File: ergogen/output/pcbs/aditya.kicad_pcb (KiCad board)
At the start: 2 copper layers, 133.2 x 110.8 mm, 58 parts

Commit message: added rgb leds!!
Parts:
- added LED1: , ceoloide:led_SK6812mini-e (per-key, reversible), B.Cu at (100.0, 104.7)
- added LED10: , ceoloide:led_SK6812mini-e (per-key, reversible), B.Cu at (172.0, 62.2)
- added LED11: , ceoloide:led_SK6812mini-e (per-key, reversible), B.Cu at (190.0, 96.2)
- added LED12: , ceoloide:led_SK6812mini-e (per-key, reversible), B.Cu at (190.0, 62.2)
- added LED13: , ceoloide:led_SK6812mini-e (per-key, reversible), B.Cu at (100.0, 87.7)
- added LED14: , ceoloide:led_SK6812mini-e (per-key, reversible), B.Cu at (100.0, 53.7)
- added LED15: , ceoloide:led_SK6812mini-e (per-key, reversible), B.Cu at (118.0, 84.3)
- added LED16: , ceoloide:led_SK6812mini-e (per-key, reversible), B.Cu at (118.0, 50.3)
- added LED17: , ceoloide:led_SK6812mini-e (per-key, reversible), B.Cu at (136.0, 79.2)
- added LED18: , ceoloide:led_SK6812mini-e (per-key, reversible), B.Cu at (136.0, 45.2)
- added LED19: , ceoloide:led_SK6812mini-e (per-key, reversible), B.Cu at (154.0, 74.1)
- added LED2: , ceoloide:led_SK6812mini-e (per-key, reversible), B.Cu at (100.0, 70.7)
- added LED20: , ceoloide:led_SK6812mini-e (per-key, reversible), B.Cu at (154.0, 40.1)
- added LED21: , ceoloide:led_SK6812mini-e (per-key, reversible), B.Cu at (172.0, 79.2)
- added LED22: , ceoloide:led_SK6812mini-e (per-key, reversible), B.Cu at (172.0, 45.2)
- added LED23: , ceoloide:led_SK6812mini-e (per-key, reversible), B.Cu at (190.0, 79.2)
- added LED24: , ceoloide:led_SK6812mini-e (per-key, reversible), B.Cu at (190.0, 45.2)
- added LED25: , ceoloide:led_SK6812mini-e (per-key, reversible), B.Cu at (163.3, 116.5)
- added LED26: , ceoloide:led_SK6812mini-e (per-key, reversible), B.Cu at (184.3, 120.0)
- added LED27: , ceoloide:led_SK6812mini-e (per-key, reversible), B.Cu at (204.4, 127.1)
- added LED3: , ceoloide:led_SK6812mini-e (per-key, reversible), B.Cu at (118.0, 101.3)
- added LED4: , ceoloide:led_SK6812mini-e (per-key, reversible), B.Cu at (118.0, 67.3)
- added LED5: , ceoloide:led_SK6812mini-e (per-key, reversible), B.Cu at (136.0, 96.2)
- added LED6: , ceoloide:led_SK6812mini-e (per-key, reversible), B.Cu at (136.0, 62.2)
- added LED7: , ceoloide:led_SK6812mini-e (per-key, reversible), B.Cu at (154.0, 91.1)
- added LED8: , ceoloide:led_SK6812mini-e (per-key, reversible), B.Cu at (154.0, 57.1)
- added LED9: , ceoloide:led_SK6812mini-e (per-key, reversible), B.Cu at (172.0, 96.2)
- moved D25 141.4 mm to (156.0, 112.8)
- moved D1 141.4 mm to (92.4, 101.6)
- moved D10 141.4 mm to (128.4, 76.1)
- moved D11 141.4 mm to (128.4, 59.1)
- moved D12 141.4 mm to (128.4, 42.1)
- moved D13 141.4 mm to (146.4, 88.0)
- moved D14 141.4 mm to (146.4, 71.0)
- moved D15 141.4 mm to (146.4, 54.0)
- moved D16 141.4 mm to (146.4, 37.0)
- moved D17 141.4 mm to (164.4, 93.1)
- moved D18 141.4 mm to (164.4, 76.1)
- moved D19 141.4 mm to (164.4, 59.1)
- moved D2 141.4 mm to (92.4, 84.6)
- moved D20 141.4 mm to (164.4, 42.1)
- moved D21 141.4 mm to (182.4, 93.1)
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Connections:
- D1 pad 1: P5 -> P18
- D10 pad 1: P4 -> P19
- D11 pad 1: P0 -> P20
- D12 pad 1: P1 -> P21
- D13 pad 1: P5 -> P18
- D14 pad 1: P4 -> P19
- D15 pad 1: P0 -> P20
- D16 pad 1: P1 -> P21
- D17 pad 1: P5 -> P18
- D18 pad 1: P4 -> P19
- D19 pad 1: P0 -> P20
- D2 pad 1: P4 -> P19
- D20 pad 1: P1 -> P21
- D21 pad 1: P5 -> P18
- D22 pad 1: P4 -> P19
- D23 pad 1: P0 -> P20
- D24 pad 1: P1 -> P21
- D25 pad 1: P7 -> P10
- D26 pad 1: P7 -> P10
- D27 pad 1: P7 -> P10
- D3 pad 1: P0 -> P20
- D4 pad 1: P1 -> P21
- D5 pad 1: P5 -> P18
- D6 pad 1: P4 -> P19
- D7 pad 1: P0 -> P20
- D8 pad 1: P1 -> P21
- D9 pad 1: P5 -> P18
- S1 pad 1: P20 -> P1
- S10 pad 1: P18 -> P4
- S11 pad 1: P18 -> P4
- S12 pad 1: P18 -> P4
- S13 pad 1: P10 -> P5
- S14 pad 1: P10 -> P5
- S15 pad 1: P10 -> P5
- S16 pad 1: P10 -> P5
- S17 pad 1: P9 -> P7
- S18 pad 1: P9 -> P7
- S19 pad 1: P9 -> P7
- S2 pad 1: P20 -> P1
- S20 pad 1: P9 -> P7
- S3 pad 1: P20 -> P1
- S4 pad 1: P20 -> P1
- S5 pad 1: P19 -> P0
- S6 pad 1: P19 -> P0
- S7 pad 1: P19 -> P0
- S8 pad 1: P19 -> P0
- S9 pad 1: P18 -> P4
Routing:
- net VCC: track 0.00 -> 101.4 mm, vias 0 -> 27
- net GND: track 0.00 -> 101.4 mm, vias 0 -> 27
- net LED_3: track 0.00 -> 13.5 mm, vias 0 -> 2
- net LED_9: track 0.00 -> 13.5 mm, vias 0 -> 2
- net LED_8: track 0.00 -> 13.5 mm, vias 0 -> 2
- net LED_7: track 0.00 -> 13.5 mm, vias 0 -> 2
- net LED_6: track 0.00 -> 13.5 mm, vias 0 -> 2
- net LED_5: track 0.00 -> 13.5 mm, vias 0 -> 2
- net LED_4: track 0.00 -> 13.5 mm, vias 0 -> 2
- net LED_26: track 0.00 -> 13.5 mm, vias 0 -> 2
- net LED_25: track 0.00 -> 13.5 mm, vias 0 -> 2
- net LED_24: track 0.00 -> 13.5 mm, vias 0 -> 2
- net LED_23: track 0.00 -> 13.5 mm, vias 0 -> 2
- net LED_22: track 0.00 -> 13.5 mm, vias 0 -> 2
- net LED_21: track 0.00 -> 13.5 mm, vias 0 -> 2
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
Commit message: ft. StackOverChonk
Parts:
- removed S28: , 434121025816
- removed T1: , Button_Switch_SMD:SW_SPDT_PCM12
- removed _2: , Connector_JST:JST_PH_S2B-PH-K_1x02_P2.00mm_Horizontal
- added BT1: , Battery_pads, F.Cu at (205.0, 71.4)
- added BT2: , Battery_pads, B.Cu at (205.0, 71.4)
- added DISP1: , ceoloide:display_ssd1306, F.Cu at (214.2, 53.2)
- added PWR1: , ceoloide:power_switch_smd_side, B.Cu at (214.2, 32.4)
- added RST1: , ceoloide:reset_switch_smd_side, F.Cu at (222.5, 71.4)
- D1, D10, D11, D12, D13, D14, D15, D16, D17, D18, D19, D2, D20, D21, D22, D23, D24, D25, D26, D27, D3, D4, D5, D6, D7, D8, D9: moved to F.Cu
- moved D25 5.02 mm to (160.7, 111.1)
- moved D11 4.87 mm to (133.0, 57.5)
- moved D12 4.87 mm to (133.0, 40.5)
- moved D15 4.87 mm to (151.0, 52.4)
- moved D16 4.87 mm to (151.0, 35.4)
- moved D19 4.87 mm to (169.0, 57.5)
- moved D20 4.87 mm to (169.0, 40.5)
- moved D4 4.87 mm to (97.0, 49.0)
- moved D8 4.87 mm to (115.0, 45.6)
- moved D1 4.87 mm to (97.0, 100.0)
- moved D10 4.87 mm to (133.0, 74.5)
- moved D13 4.87 mm to (151.0, 86.4)
- moved D14 4.87 mm to (151.0, 69.4)
- moved D17 4.87 mm to (169.0, 91.5)
- moved D18 4.87 mm to (169.0, 74.5)
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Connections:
- D25 pad 1: P10 -> P7
- D26 pad 1: P10 -> P7
- D27 pad 1: P10 -> P7
- MCU1 pad 101: P1 -> RAW
- MCU1 pad 102: P0 -> GND
- MCU1 pad 103: GND -> RST
- MCU1 pad 104: GND -> VCC
- MCU1 pad 105: P2 -> P21
- MCU1 pad 106: P3 -> P20
- MCU1 pad 107: P4 -> P19
- MCU1 pad 108: P5 -> P18
- MCU1 pad 109: P6 -> P15
- MCU1 pad 110: P7 -> P14
- MCU1 pad 111: P8 -> P16
- MCU1 pad 112: P9 -> P10
- MCU1 pad 113: P10 -> P9
- MCU1 pad 114: P16 -> P8
- MCU1 pad 115: P14 -> P7
- MCU1 pad 116: P15 -> P6
- MCU1 pad 117: P18 -> P5
- MCU1 pad 118: P19 -> P4
- MCU1 pad 119: P20 -> P3
- MCU1 pad 120: P21 -> P2
- MCU1 pad 121: VCC -> GND
- MCU1 pad 122: RST -> GND
- MCU1 pad 123: GND -> P0
- MCU1 pad 124: RAW -> P1
- S1 pad 1: P1 -> matrix_outer_down
- S1 pad 2: matrix_outer_down -> P1
- S10 pad 1: P4 -> matrix_ring_home
- S10 pad 2: matrix_ring_home -> P4
- S11 pad 1: P4 -> matrix_ring_up
- S11 pad 2: matrix_ring_up -> P4
- S12 pad 1: P4 -> matrix_ring_num
- S12 pad 2: matrix_ring_num -> P4
- S13 pad 1: P5 -> matrix_middle_down
- S13 pad 2: matrix_middle_down -> P5
- S14 pad 1: P5 -> matrix_middle_home
- S14 pad 2: matrix_middle_home -> P5
- S15 pad 1: P5 -> matrix_middle_up
- S15 pad 2: matrix_middle_up -> P5
- S16 pad 1: P5 -> matrix_middle_num
- S16 pad 2: matrix_middle_num -> P5
- S17 pad 1: P7 -> matrix_index_down
- S17 pad 2: matrix_index_down -> P7
- S18 pad 1: P7 -> matrix_index_home
- S18 pad 2: matrix_index_home -> P7
- S19 pad 1: P7 -> matrix_index_up
- S19 pad 2: matrix_index_up -> P7
- S2 pad 1: P1 -> matrix_outer_home
- S2 pad 2: matrix_outer_home -> P1
- S20 pad 1: P7 -> matrix_index_num
- S20 pad 2: matrix_index_num -> P7
- S21 pad 1: P8 -> matrix_inner_down
- S21 pad 2: matrix_inner_down -> P8
- S22 pad 1: P8 -> matrix_inner_home
- S22 pad 2: matrix_inner_home -> P8
- S23 pad 1: P8 -> matrix_inner_up
- S23 pad 2: matrix_inner_up -> P8
- S24 pad 1: P8 -> matrix_inner_num
- S24 pad 2: matrix_inner_num -> P8
- S25 pad 1: P7 -> thumbs_col1_cluster
- S25 pad 2: thumbs_col1_cluster -> P5
- S26 pad 1: P8 -> thumbs_col2_cluster
- S26 pad 2: thumbs_col2_cluster -> P7
- S27 pad 1: P9 -> thumbs_col3_cluster
- S27 pad 2: thumbs_col3_cluster -> P8
- S3 pad 1: P1 -> matrix_outer_up
- S3 pad 2: matrix_outer_up -> P1
- S4 pad 1: P1 -> matrix_outer_num
- S4 pad 2: matrix_outer_num -> P1
- S5 pad 1: P0 -> matrix_pinky_down
- S5 pad 2: matrix_pinky_down -> P0
- S6 pad 1: P0 -> matrix_pinky_home
- S6 pad 2: matrix_pinky_home -> P0
- S7 pad 1: P0 -> matrix_pinky_up
- S7 pad 2: matrix_pinky_up -> P0
- S8 pad 1: P0 -> matrix_pinky_num
- S8 pad 2: matrix_pinky_num -> P0
- S9 pad 1: P4 -> matrix_ring_down
- S9 pad 2: matrix_ring_down -> P4
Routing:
- net P7: track 0.00 -> 40.1 mm, vias 0 -> 8
- net P5: track 0.00 -> 33.5 mm, vias 0 -> 5
- net P8: track 0.00 -> 33.5 mm, vias 0 -> 5
- net P4: track 0.00 -> 26.8 mm, vias 0 -> 4
- net P1: track 0.00 -> 26.8 mm, vias 0 -> 4
- net P0: track 0.00 -> 26.8 mm, vias 0 -> 4
- net P19: track 0.00 -> 13.2 mm, vias 0 -> 6
- net P18: track 0.00 -> 13.2 mm, vias 0 -> 6
- net P20: track 0.00 -> 13.2 mm, vias 0 -> 6
- net P21: track 0.00 -> 13.2 mm, vias 0 -> 6
- net thumbs_col1_cluster: track 0.00 -> 8.90 mm, vias 0 -> 2
- net matrix_ring_home: track 0.00 -> 8.90 mm, vias 0 -> 2
- net matrix_ring_down: track 0.00 -> 8.90 mm, vias 0 -> 2
- net matrix_pinky_home: track 0.00 -> 8.90 mm, vias 0 -> 2
- net matrix_pinky_down: track 0.00 -> 8.90 mm, vias 0 -> 2
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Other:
- board size 133.2 x 110.8 mm -> 138.9 x 113.2 mm
- board text added: "StackOverChonk - v0.1 pre-release github.com/im-AMS/StackOverChonk"
- board text removed: "A keyboard for Aditya"

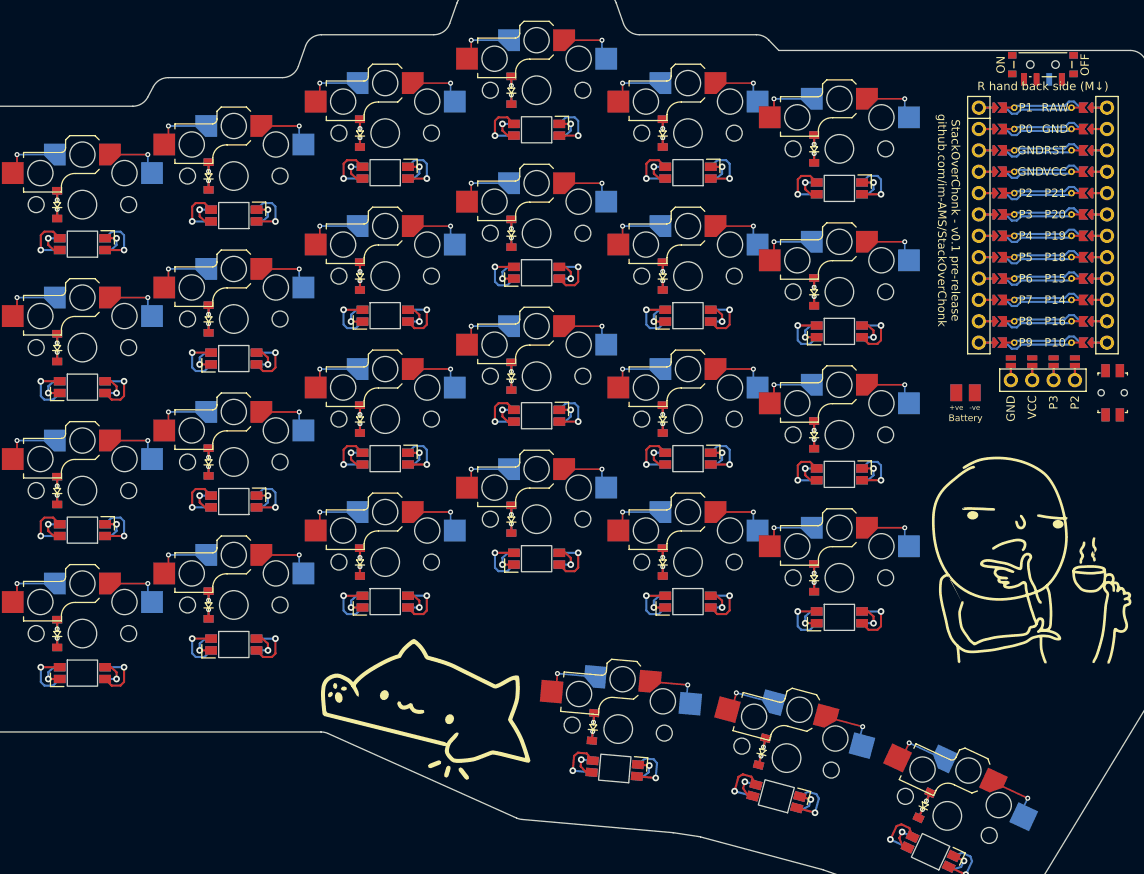
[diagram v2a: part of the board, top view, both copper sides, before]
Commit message: fixed cluster pins
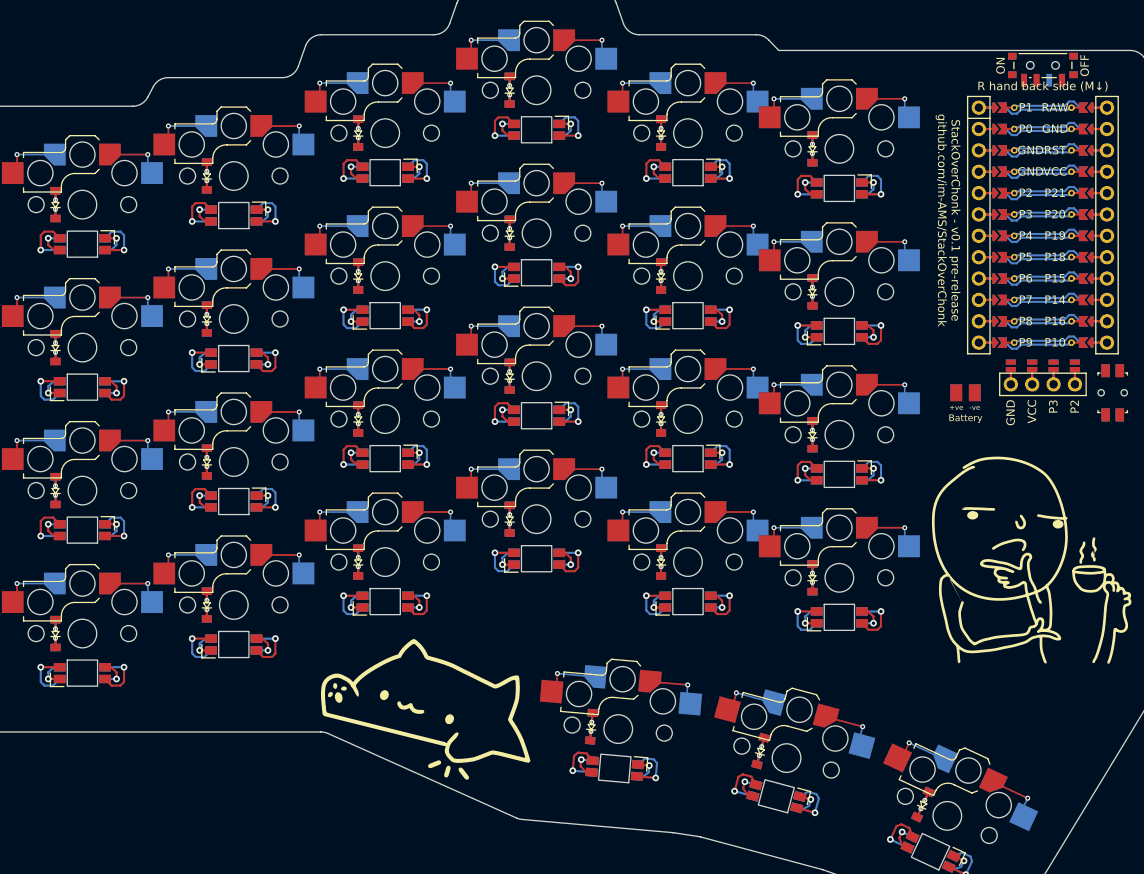
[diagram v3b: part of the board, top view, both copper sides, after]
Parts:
- moved DISP1 0.50 mm to (214.2, 53.7)
- moved D1 0.20 mm to (96.8, 100.0)
- moved D2 0.20 mm to (96.8, 83.0)
- moved D3 0.20 mm to (96.8, 66.0)
- moved D4 0.20 mm to (96.8, 49.0)
- moved D5 0.20 mm to (114.8, 96.6)
- moved D6 0.20 mm to (114.8, 79.6)
- moved D7 0.20 mm to (114.8, 62.6)
- moved D8 0.20 mm to (114.8, 45.6)
- moved D10 0.20 mm to (132.8, 74.5)
- moved D11 0.20 mm to (132.8, 57.5)
- moved D12 0.20 mm to (132.8, 40.5)
- moved D13 0.20 mm to (150.8, 86.4)
- moved D14 0.20 mm to (150.8, 69.4)
- moved D15 0.20 mm to (150.8, 52.4)
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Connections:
- D25 pad 1: P7 -> P15
- D26 pad 1: P7 -> P15
- D27 pad 1: P7 -> P15
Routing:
- net P7: track 40.1 -> 33.5 mm, vias 8 -> 5
- net P15: track 0.00 -> 6.60 mm, vias 0 -> 3

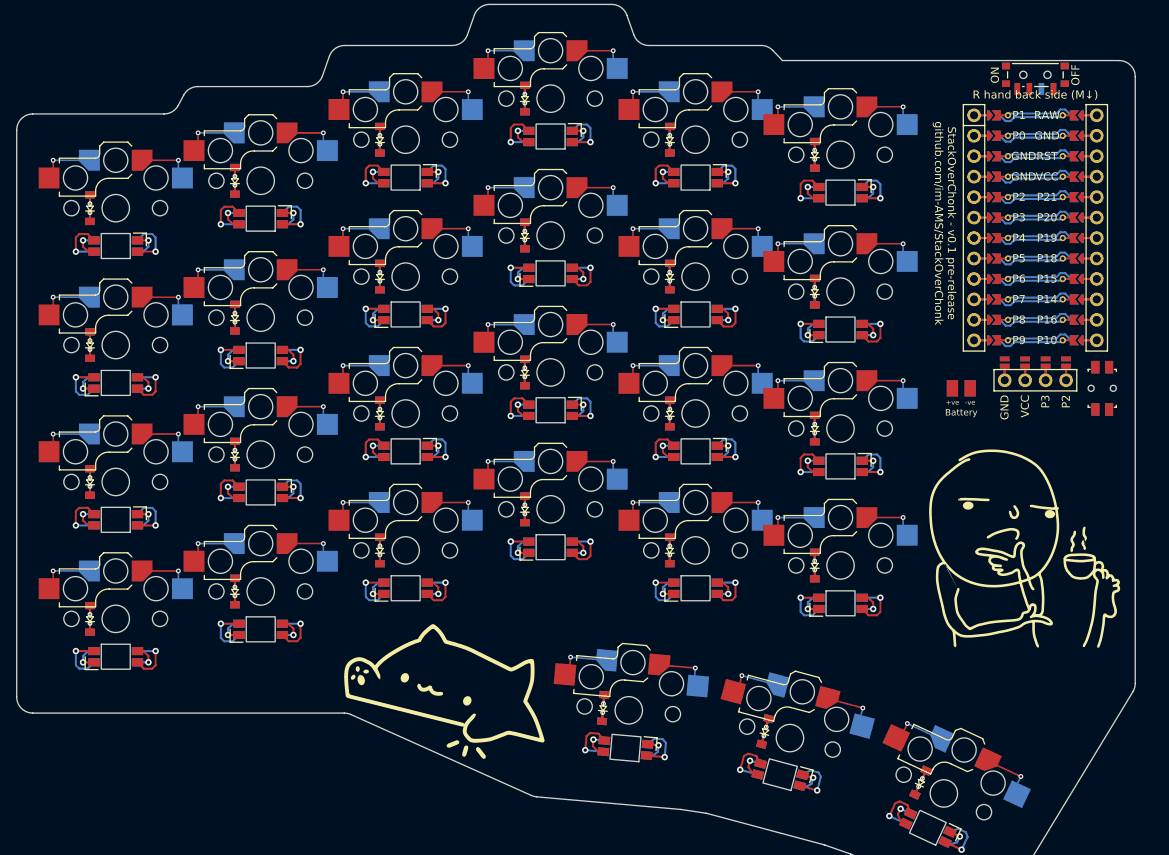
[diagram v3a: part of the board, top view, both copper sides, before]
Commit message: fix diode positoning and multiple others
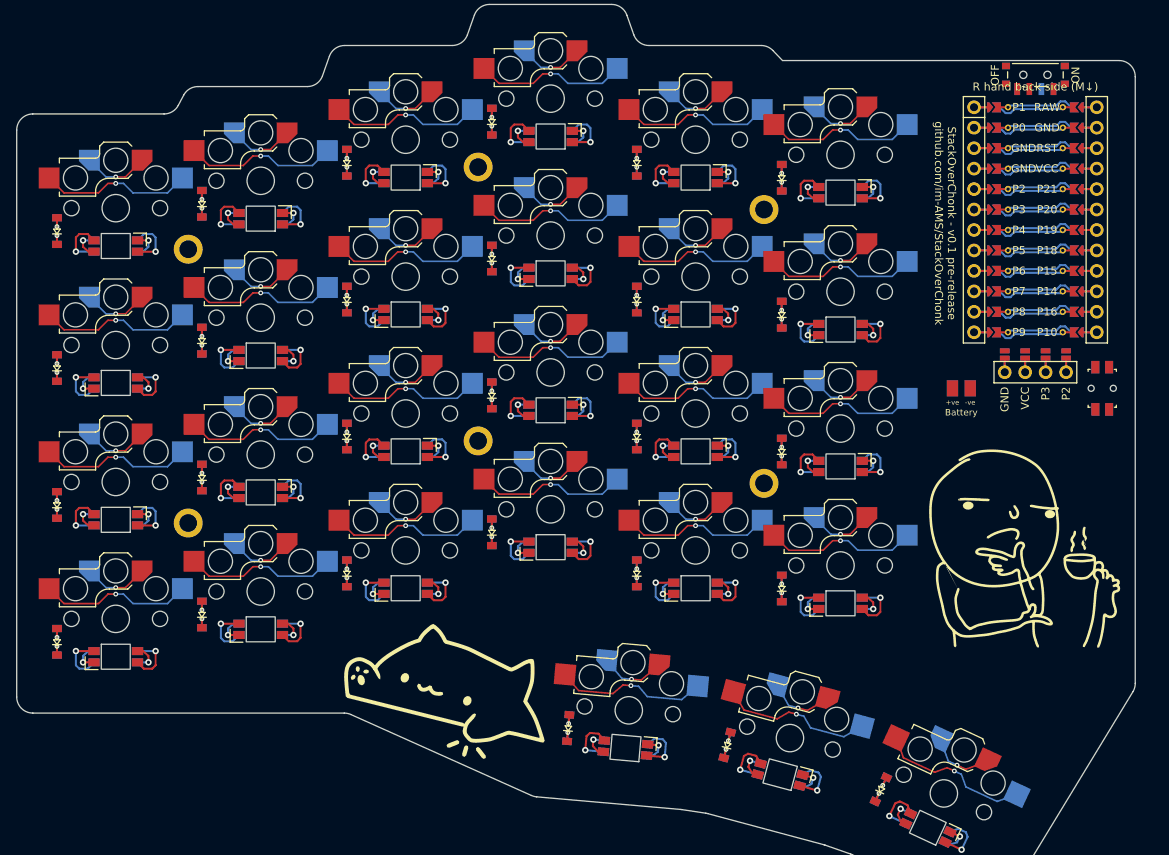
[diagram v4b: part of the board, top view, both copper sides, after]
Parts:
- added H1: , ceoloide:mounting_hole_plated, B.Cu at (109.0, 54.1)
- added H2: , ceoloide:mounting_hole_plated, B.Cu at (109.0, 88.1)
- added H3: , ceoloide:mounting_hole_plated, B.Cu at (180.5, 49.2)
- added H4: , ceoloide:mounting_hole_plated, B.Cu at (180.5, 83.2)
- added H5: , ceoloide:mounting_hole_plated, B.Cu at (145.0, 77.9)
- added H6: , ceoloide:mounting_hole_plated, B.Cu at (145.0, 43.9)
- LED1, LED10, LED11, LED12, LED13, LED14, LED15, LED16, LED17, LED18, LED19, LED2, LED20, LED21, LED22, LED23, LED24, LED25, LED26, LED27, LED3, LED4, LED5, LED6, LED7, LED8, LED9: moved to F.Cu
- moved D25 4.99 mm to (156.2, 113.6)
- moved D26 4.99 mm to (175.9, 115.7)
- moved D27 4.99 mm to (195.0, 121.2)
- moved D11 4.99 mm to (128.7, 60.4)
- moved D12 4.99 mm to (128.7, 43.4)
- moved D15 4.99 mm to (146.7, 55.3)
- moved D16 4.99 mm to (146.7, 38.3)
- moved D19 4.99 mm to (164.7, 60.4)
- moved D20 4.99 mm to (164.7, 43.4)
- moved D23 4.99 mm to (182.7, 62.2)
- moved D24 4.99 mm to (182.7, 45.2)
- moved D10 4.99 mm to (128.7, 77.3)
- moved D13 4.99 mm to (146.7, 89.2)
- moved D14 4.99 mm to (146.7, 72.2)
- moved D17 4.99 mm to (164.7, 94.3)
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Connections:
- S1 pad 1: matrix_outer_down -> P1
- S1 pad 2: P1 -> matrix_outer_down
- S10 pad 1: matrix_ring_home -> P4
- S10 pad 2: P4 -> matrix_ring_home
- S11 pad 1: matrix_ring_up -> P4
- S11 pad 2: P4 -> matrix_ring_up
- S12 pad 1: matrix_ring_num -> P4
- S12 pad 2: P4 -> matrix_ring_num
- S13 pad 1: matrix_middle_down -> P5
- S13 pad 2: P5 -> matrix_middle_down
- S14 pad 1: matrix_middle_home -> P5
- S14 pad 2: P5 -> matrix_middle_home
- S15 pad 1: matrix_middle_up -> P5
- S15 pad 2: P5 -> matrix_middle_up
- S16 pad 1: matrix_middle_num -> P5
- S16 pad 2: P5 -> matrix_middle_num
- S17 pad 1: matrix_index_down -> P7
- S17 pad 2: P7 -> matrix_index_down
- S18 pad 1: matrix_index_home -> P7
- S18 pad 2: P7 -> matrix_index_home
- S19 pad 1: matrix_index_up -> P7
- S19 pad 2: P7 -> matrix_index_up
- S2 pad 1: matrix_outer_home -> P1
- S2 pad 2: P1 -> matrix_outer_home
- S20 pad 1: matrix_index_num -> P7
- S20 pad 2: P7 -> matrix_index_num
- S21 pad 1: matrix_inner_down -> P8
- S21 pad 2: P8 -> matrix_inner_down
- S22 pad 1: matrix_inner_home -> P8
- S22 pad 2: P8 -> matrix_inner_home
- S23 pad 1: matrix_inner_up -> P8
- S23 pad 2: P8 -> matrix_inner_up
- S24 pad 1: matrix_inner_num -> P8
- S24 pad 2: P8 -> matrix_inner_num
- S25 pad 1: thumbs_col1_cluster -> P5
- S25 pad 2: P5 -> thumbs_col1_cluster
- S26 pad 1: thumbs_col2_cluster -> P7
- S26 pad 2: P7 -> thumbs_col2_cluster
- S27 pad 1: thumbs_col3_cluster -> P8
- S27 pad 2: P8 -> thumbs_col3_cluster
- S3 pad 1: matrix_outer_up -> P1
- S3 pad 2: P1 -> matrix_outer_up
- S4 pad 1: matrix_outer_num -> P1
- S4 pad 2: P1 -> matrix_outer_num
- S5 pad 1: matrix_pinky_down -> P0
- S5 pad 2: P0 -> matrix_pinky_down
- S6 pad 1: matrix_pinky_home -> P0
- S6 pad 2: P0 -> matrix_pinky_home
- S7 pad 1: matrix_pinky_up -> P0
- S7 pad 2: P0 -> matrix_pinky_up
- S8 pad 1: matrix_pinky_num -> P0
- S8 pad 2: P0 -> matrix_pinky_num
- S9 pad 1: matrix_ring_down -> P4
- S9 pad 2: P4 -> matrix_ring_down
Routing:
- net thumbs_col3_cluster: track 8.90 -> 21.3 mm
- net matrix_pinky_up: track 8.90 -> 21.3 mm
- net matrix_pinky_num: track 8.90 -> 21.3 mm
- net matrix_pinky_home: track 8.90 -> 21.3 mm
- net matrix_pinky_down: track 8.90 -> 21.3 mm
- net matrix_outer_up: track 8.90 -> 21.3 mm
- net matrix_outer_num: track 8.90 -> 21.3 mm
- net matrix_outer_home: track 8.90 -> 21.3 mm
- net matrix_outer_down: track 8.90 -> 21.3 mm
- net matrix_middle_num: track 8.90 -> 21.3 mm
- net matrix_ring_up: track 8.90 -> 21.3 mm
- net matrix_ring_num: track 8.90 -> 21.3 mm
- net matrix_ring_home: track 8.90 -> 21.3 mm
- net matrix_ring_down: track 8.90 -> 21.3 mm
- net matrix_middle_up: track 8.90 -> 21.3 mm
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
